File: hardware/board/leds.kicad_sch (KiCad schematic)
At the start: 7 parts, among them U3 TL074

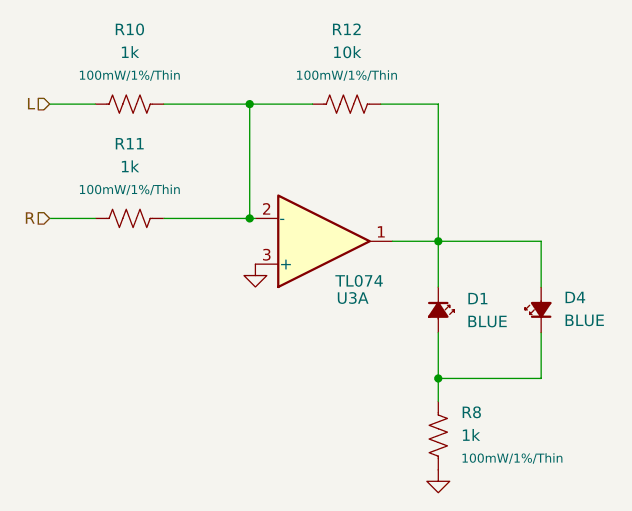
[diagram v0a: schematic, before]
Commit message: Hardware v10:
- Replaced EOL 5V DC-DC converter with new TI part.
- Re-drawn schematic to current Winterbloom standards and style.
- Improved layout and color-coding.
- Updated branding and silk screen.
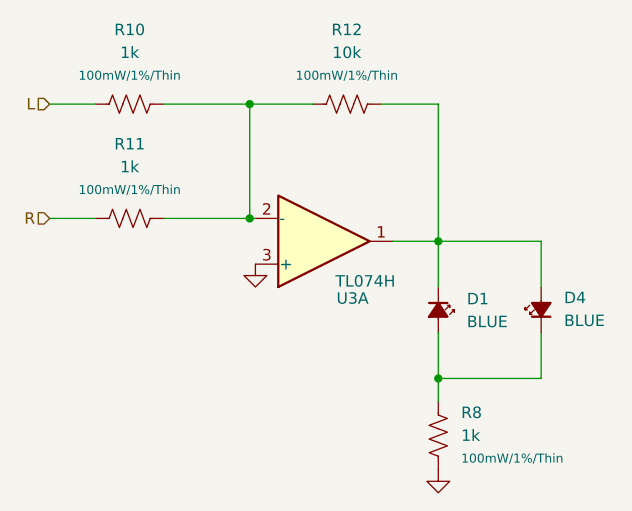
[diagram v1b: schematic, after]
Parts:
- R10, R11, R8: DigiKey YAG2323TR-ND -> (none)
- R12: DigiKey YAG2323TR-ND -> (none); LCSC C375503 -> C469659; MPN RT0603FRE071KL -> RT0603FRE0710KL
- U3: value TL074 -> TL074H; Substitutes Allowed (none) -> No; mpn TL074CPW -> (none); populate 1 -> (none)
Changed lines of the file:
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@@
 	(title_block
 		(title "Speak to Me")
-		(date "2024-07-21")
-		(rev "v9")
+		(date "2024-08-28")
+		(rev "v10")
 		(company "Winterbloom")
 		(comment 1 "Alethea Flowers")
@@
 			)
 		)
-		(property "DigiKey" "YAG2323TR-ND"
+		(property "DigiKey" ""
 			(at 64.77 67.31 0)
 			(effects
@@
 		)
 		(property "MPN" "RT0603FRE071KL"
-			(at 64.77 67.31 0)
-			(effects
-				(font
-					(size 1.27 1.27)
-				)
-				(hide yes)
-			)
-		)
-		(property "search link" ""
 			(at 64.77 67.31 0)
 			(effects
@@
 			)
 		)
-		(property "search link" ""
-			(at 99.06 90.17 0)
-			(effects
-				(font
-					(size 1.27 1.27)
-				)
-				(hide yes)
-			)
-		)
 		(pin "1"
 		)
@@
 			)
 		)
-		(property "Value" "TL074"
+		(property "Value" "TL074H"
 			(at 87.63 86.995 0)
 			(effects
@@
 			)
 		)
-		(property "mpn" "TL074CPW"
-			(at 86.36 90.17 0)
-			(effects
-				(font
-					(size 1.27 1.27)
-				)
-				(hide yes)
-			)
-		)
-		(property "populate" "1"
-			(at 86.36 82.55 0)
-			(effects
-				(font
-					(size 1.27 1.27)
-				)
-				(hide yes)
-			)
-		)
 		(property "Rating" ""
 			(at 86.36 82.55 0)
@@
 			)
 		)
-		(property "search link" ""
+		(property "Substitutes Allowed" "No"
 			(at 86.36 82.55 0)
 			(effects
@@
 			)
 		)
-		(property "DigiKey" "YAG2323TR-ND"
+		(property "DigiKey" ""
 			(at 99.06 104.14 0)
 			(effects
@@
 		)
 		(property "MPN" "RT0603FRE071KL"
-			(at 99.06 104.14 0)
-			(effects
-				(font
-					(size 1.27 1.27)
-				)
-				(hide yes)
-			)
-		)
-		(property "search link" ""
 			(at 99.06 104.14 0)
 			(effects
@@
 			)
 		)
-		(property "DigiKey" "YAG2323TR-ND"
+		(property "DigiKey" ""
 			(at 88.9 67.31 0)
 			(effects
@@
 			)
 		)
-		(property "LCSC" "C375503"
+		(property "LCSC" "C469659"
 			(at 88.9 67.31 0)
 			(effects
@@
 			)
 		)
-		(property "MPN" "RT0603FRE071KL"
-			(at 88.9 67.31 0)
-			(effects
-				(font
-					(size 1.27 1.27)
-				)
-				(hide yes)
-			)
-		)
-		(property "search link" ""
+		(property "MPN" "RT0603FRE0710KL"
 			(at 88.9 67.31 0)
 			(effects
@@
 			)
 		)
-		(property "DigiKey" "YAG2323TR-ND"
+		(property "DigiKey" ""
 			(at 64.77 80.01 0)
 			(effects
@@
 		)
 		(property "MPN" "RT0603FRE071KL"
-			(at 64.77 80.01 0)
-			(effects
-				(font
-					(size 1.27 1.27)
-				)
-				(hide yes)
-			)
-		)
-		(property "search link" ""
 			(at 64.77 80.01 0)
 			(effects
@@
 			(at 110.49 90.17 0)
 			(effects
-				(font
-					(size 1.27 1.27)
-				)
-				(hide yes)
-			)
-		)
-		(property "search link" ""
-			(at 110.49 90.17 0)
-			(effects
